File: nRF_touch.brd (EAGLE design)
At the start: 46.5 x 82.7 mm, 91 parts, among them IC1 MCP73831/OT, Q1 BSS138BKW, T1 BSS84, T2 BC847, T3 BC847, T4 BC847, U1 ADP160, U2 AT42QT1040, Y1 32.768kHz, Y2 32MHz-3.2X2.5

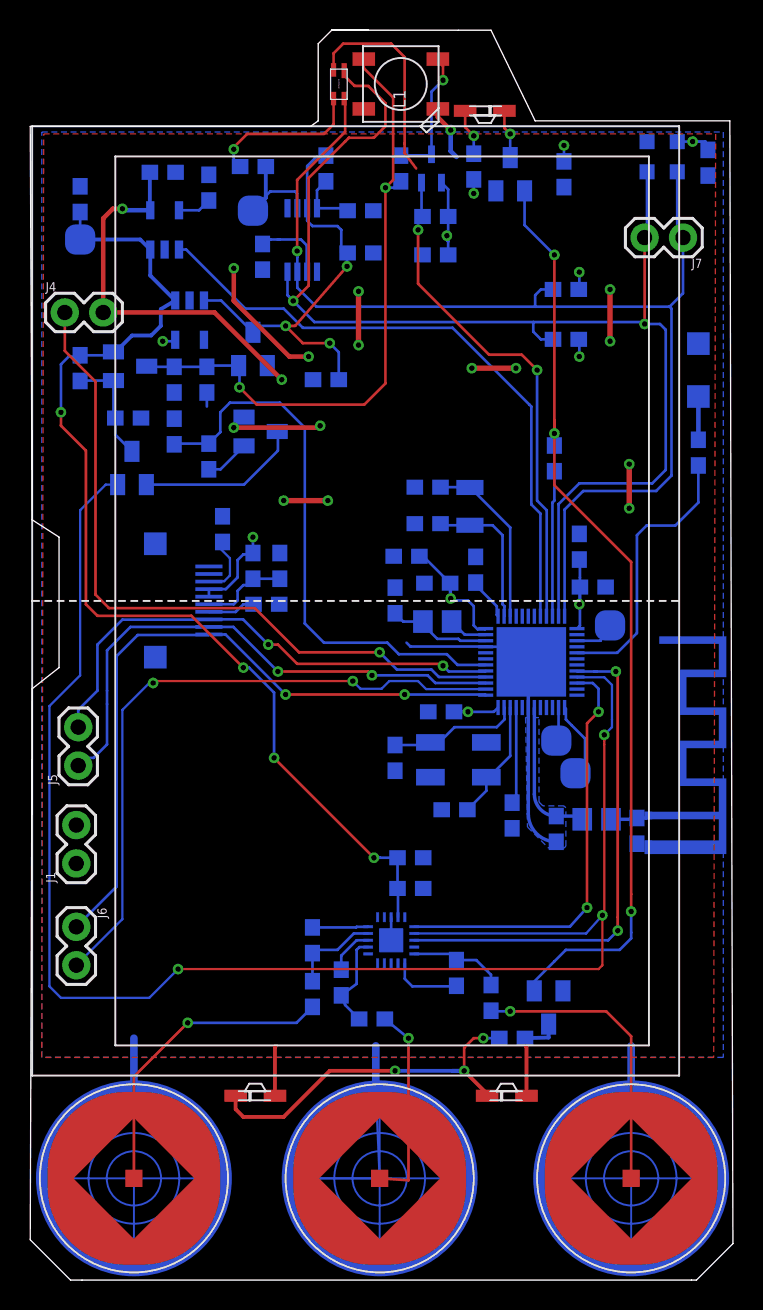
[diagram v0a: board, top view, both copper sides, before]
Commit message: -Same dimensions for top and bottom -more pads exposed -different power distribution
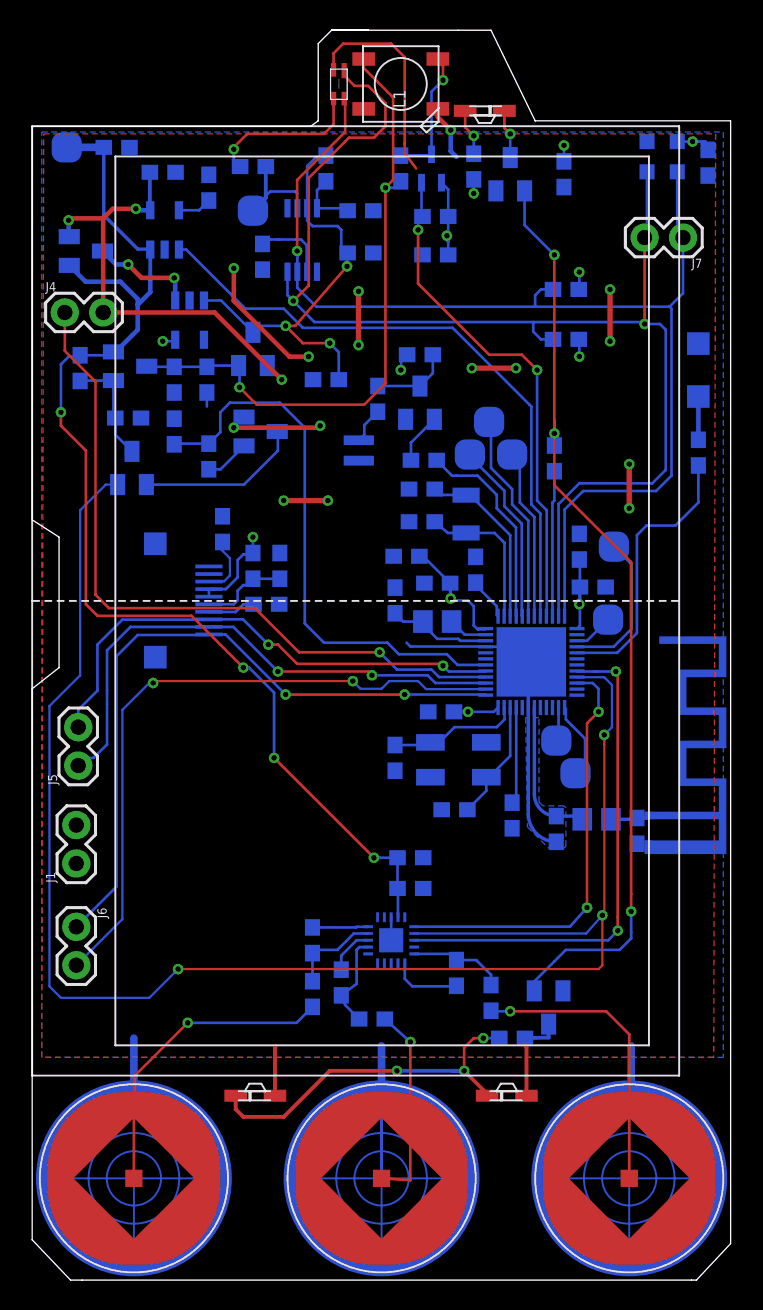
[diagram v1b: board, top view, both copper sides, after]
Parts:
- added C30: 1uF, SparkFun-Capacitors:0603
- added D1: BAT54C, nxp_60:SOT23
- added P13, P4, P5: TESTPOINT_22, test_points:TESTPOINT_22
- added P3: p3, test_points:TESTPOINT_22
- added R24: 1k, SparkFun-Resistors:0603
- added R25: 330, SparkFun-Resistors:0603
- added SPK1: s1, Strutz Electronic Industries:IND-2020
- added T5: BC847, nxp_60:SOT23
- FB1: value FB_0805 -> 25uH 0805
- moved VBAT 6.16 mm to (2.29, 72.3)
- moved C8 4.19 mm to (5.59, 72.3), turned to 180 degrees
- moved Y1 0.57 mm to (28.7, 48.0)
- moved C21 0.40 mm to (25.8, 49.7)
- moved C20 0.40 mm to (25.8, 47.5)
- moved RX 0.40 mm to (38.1, 41.0)
- moved S1 0.13 mm to (39.5, 4.06)
- moved S2 0.13 mm to (23.1, 4.06), turned to 90 degrees
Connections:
- new net LDO_VIN: D1.3, U1.1
- new net N$10: C30.1, R25.2, T5.3
- new net N$29: C30.2, SPK1.P$1
- new net N$30: R24.1, T5.1
- new net P13: P13.P$1, U$6.16
- new net P2: R24.2, U$6.4
- new net P3: P3.P$1, U$6.5
- new net P4: P4.P$1, U$6.6
- new net P5: P5.P$1, U$6.7
- net GND: now also SPK1.P$2, T5.2
- net VBAT: now also D1.1; no longer U1.1
- net VCC: now also R25.1
- net VUSB: now also D1.2
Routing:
- net P4: track 0.00 -> 13.9 mm
- net P2: track 0.00 -> 13.5 mm
- net P3: track 0.00 -> 12.1 mm
- net P5: track 0.00 -> 11.3 mm
- net P13: track 0.00 -> 10.00 mm
- net VBAT: track 72.1 -> 79.9 mm
- net LDO_VIN: track 0.00 -> 7.00 mm, vias 0 -> 2
- net N$10: track 0.00 -> 5.22 mm
- net VUSB: track 27.1 -> 30.6 mm, vias 2 -> 3
- net N$30: track 0.00 -> 3.35 mm
- net N$29: track 0.00 -> 2.41 mm
- net VCC: track 58.7 -> 59.9 mm, vias 11 -> 12
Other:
- board size 46.5 x 82.7 mm -> 46.2 x 82.7 mm

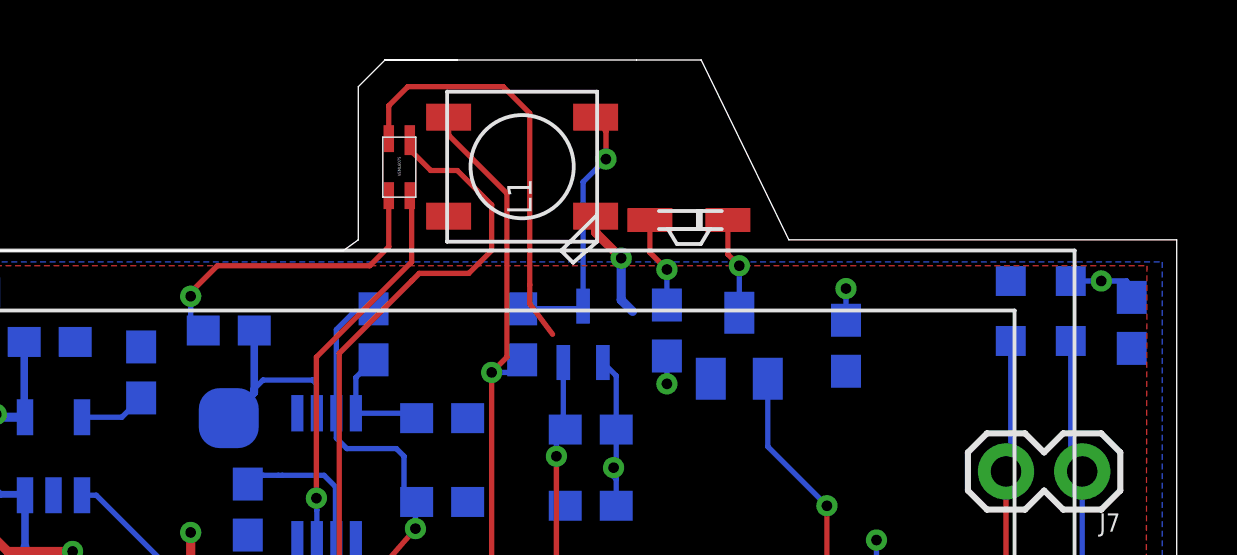
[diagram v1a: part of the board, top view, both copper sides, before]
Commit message: Remodelled neopixel PCB part
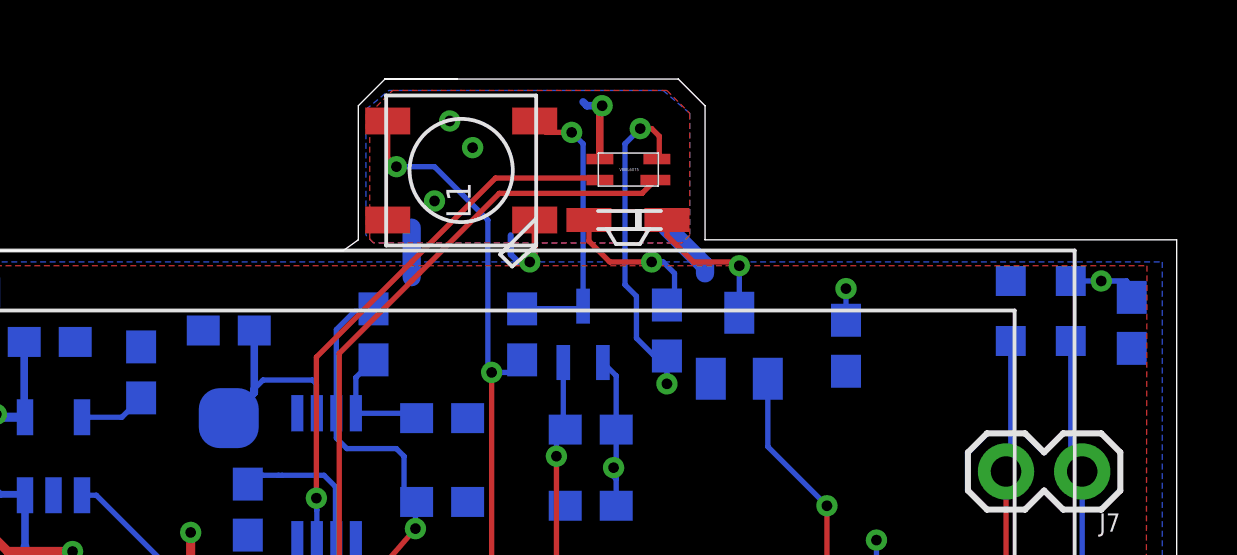
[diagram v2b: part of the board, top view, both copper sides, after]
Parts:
- moved U$2 7.10 mm to (26.9, 76.7), turned to 0 degrees
- moved L1 2.04 mm to (22.4, 76.3)
- moved U$8 2.03 mm to (29.2, 74.7)
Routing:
- net GND: track 100.8 -> 95.6 mm, vias 16 -> 19
- net SDA: track 76.8 -> 82.1 mm
- net VCC: track 59.9 -> 56.0 mm, vias 12 -> 13
- net N$11: track 3.07 -> 5.16 mm
- net N$22: track 3.25 -> 4.91 mm
- net SCL: track 85.3 -> 86.4 mm
- net SW_AT: track 42.0 -> 43.0 mm, vias 2 -> 3
- net NEO_DIN: track 10.7 -> 11.4 mm
- added copper zone on layer 1, net GND
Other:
- board size 46.2 x 82.7 mm -> 46.2 x 82 mm

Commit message: Routing done
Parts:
- removed D1: BAT54C, nxp_60:SOT23
- removed J1, J4, J5, J6, J7: (no value), SparkFun-Connectors:1X02
- removed P3: p3, test_points:TESTPOINT_22
- removed P4: TESTPOINT_22, test_points:TESTPOINT_22
- removed R10: 10k, SparkFun-Resistors:0603
- removed R20: 47k, SparkFun-Resistors:0603
- removed R9: 100k, SparkFun-Resistors:0603
- removed T2: BC847, nxp_60:SOT23
- added CONN2: 503480-1200, MOLEX12:503480-1200
- C9: value 0.1uF -> 4.7uF
- R19: value 0.010 -> 0.1
- moved C3 6.19 mm to (19.1, 70.9)
- moved R2 6.14 mm to (21.3, 65.0), turned to 270 degrees
- moved C8 5.42 mm to (2.16, 68.1), turned to 270 degrees
- moved U1 2.74 mm to (7.87, 61.8), turned to 270 degrees
- moved MBAT 1.40 mm to (14.7, 69.5), turned to 180 degrees
- moved R19 1.15 mm to (14.7, 72.1)
- moved VBAT 0.90 mm to (2.16, 71.4), turned to 0 degrees
- moved C5 0.51 mm to (21.2, 68.1)
- moved C27 0.38 mm to (25.1, 45.2)
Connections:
- net N$15 renamed DEC3
- removed net LDO_VIN: D1.3, U1.1
- removed net N$1: R9.2, T2.1
- removed net P3: P3.P$1, U$6.5
- removed net TRANS: D3.1, T2.3
- new net AT42_EN: D3.2, U2.P14
- new net STC_EN: D3.1, U$3.IO
- net 5150_CS: now also CONN2.P$10; no longer J4.1
- net AT42_COUT: now also CONN2.P$1; no longer D3.2
- net GND: now also CONN2.P$6; no longer J1.1, R10.2, R20.2, T2.2
- net P4: now also CONN2.P$3; no longer P4.P$1
- net SCL: now also CONN2.P$4; no longer J7.2
- net SDA: now also CONN2.P$5; no longer J7.1
- net SELF_EN: now also U2.P1; no longer R10.1, R9.1
- net SHARP_CS: now also CONN2.P$7; no longer J5.2
- net SPIM_DIN: now also CONN2.P$2; no longer J6.2
- net SPIM_DO: now also CONN2.P$8; no longer J5.1
- net SPIM_SCK: now also CONN2.P$9; no longer J6.1
- net SW_AT: no longer L1.1-VDD, R14.2
- net SW_POWER: now also L1.1-VDD, R14.2, U1.1; no longer C3.1, R2.2, R20.1, U$3.VCC
- net VBAT: now also C3.1, R2.2, U$3.VCC; no longer D1.1
- net VCC: now also CONN2.P$11; no longer J1.2
- net VUSB: now also CONN2.P$12; no longer D1.2, J4.2
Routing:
- net AT42_EN: track 0.00 -> 68.8 mm, vias 0 -> 2
- net AT42_COUT: track 107.6 -> 59.6 mm, vias 3 -> 2
- net SDA: track 82.1 -> 126.5 mm, vias 1 -> 3
- net SCL: track 86.4 -> 130.2 mm, vias 2 -> 5
- net VBAT: track 79.9 -> 118.6 mm, vias 4 -> 2
- net SW_AT: track 43.0 -> 6.13 mm, vias 3 -> 0
- net P4: track 13.9 -> 50.3 mm, vias 0 -> 2
- net VUSB: track 30.6 -> 58.7 mm
- net STC_EN: track 0.00 -> 23.6 mm, vias 0 -> 2
- net SPIM_DIN: track 43.6 -> 26.5 mm
- net 5150_CS: track 47.6 -> 31.6 mm, vias 1 -> 2
- net SW_POWER: track 29.9 -> 42.8 mm
- net P3: track 12.1 -> 0.00 mm
- net TRANS: track 10.9 -> 0.00 mm
- net SPIM_SCK: track 45.7 -> 36.1 mm
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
